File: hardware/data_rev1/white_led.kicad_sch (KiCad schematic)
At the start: 82 parts, among them U3 IS31FL3236A-TQ, U4 IS31FL3236A-TQ

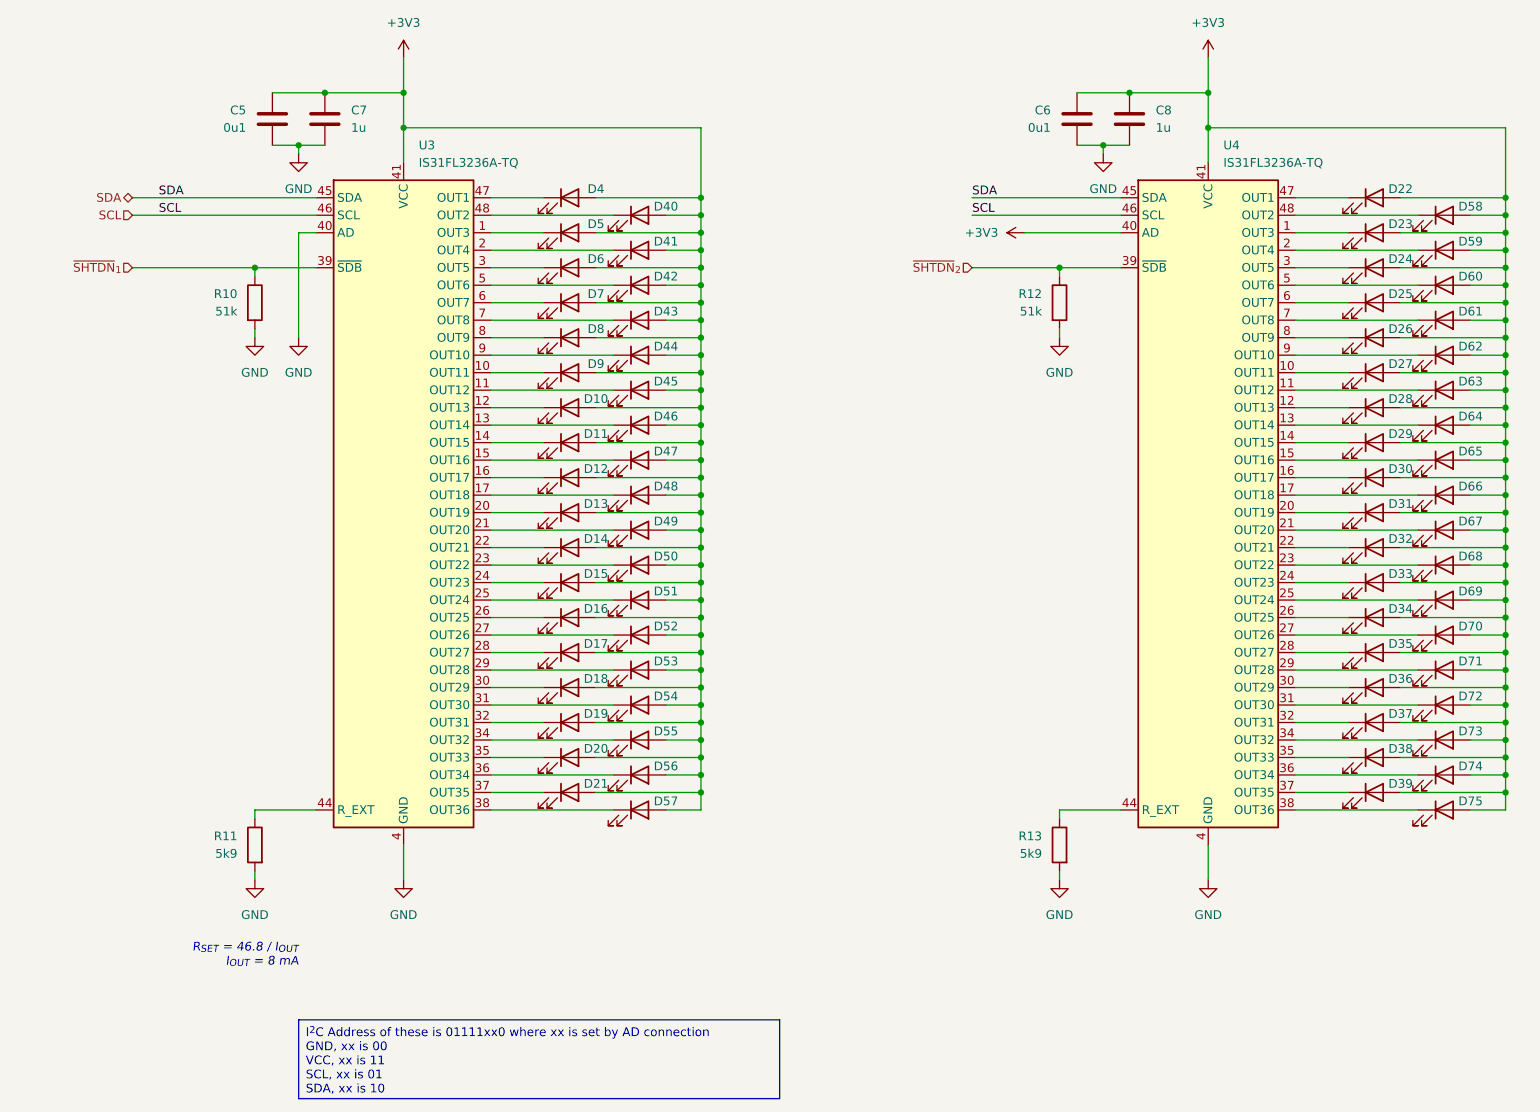
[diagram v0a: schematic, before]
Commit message: Added labels for LED lines
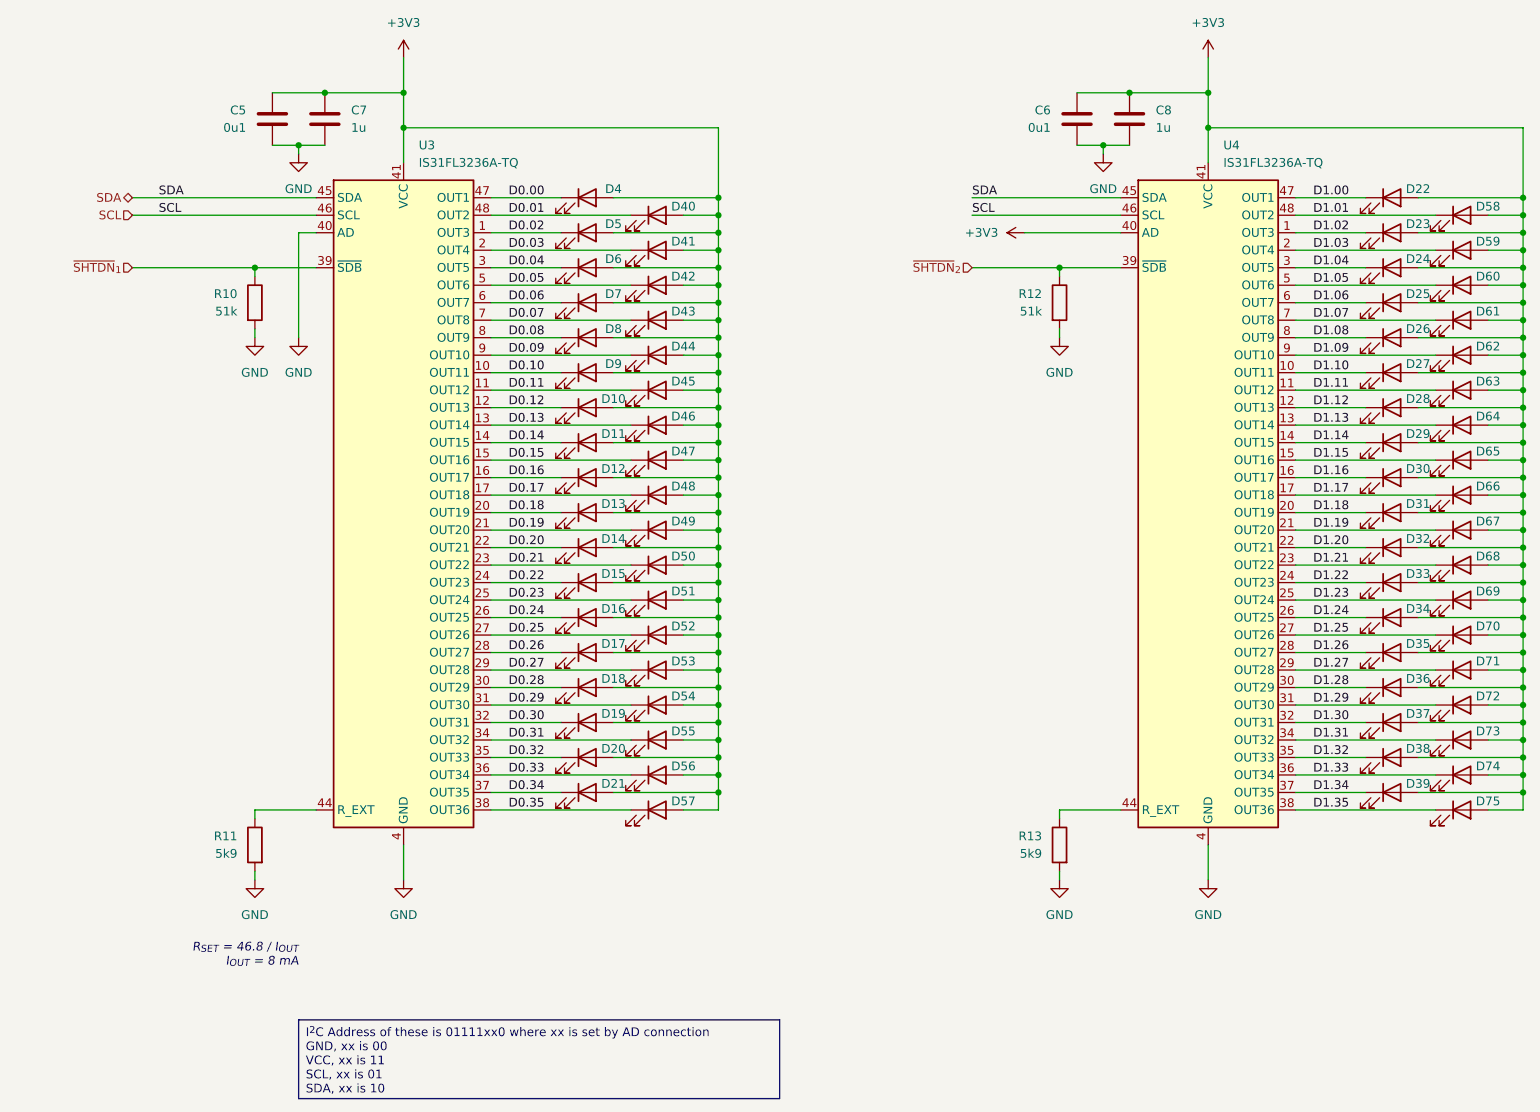
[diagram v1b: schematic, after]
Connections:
- net D0.19: now reaches D49.1 (K), U3.21 (OUT20)
- net D1.12: now reaches D28.1 (K), U4.12 (OUT13)
- net D0.20: now reaches D14.1 (K), U3.22 (OUT21)
- net D0.00: now reaches D4.1 (K), U3.47 (OUT1)
- net D0.11: now reaches D45.1 (K), U3.11 (OUT12)
- net D0.15: now reaches D47.1 (K), U3.15 (OUT16)
- net D1.09: now reaches D62.1 (K), U4.9 (OUT10)
- net D1.23: now reaches D69.1 (K), U4.25 (OUT24)
- net D1.25: now reaches D70.1 (K), U4.27 (OUT26)
- net D1.34: now reaches D39.1 (K), U4.37 (OUT35)
- net D1.00: now reaches D22.1 (K), U4.47 (OUT1)
- net D0.01: now reaches D40.1 (K), U3.48 (OUT2)
- net D1.03: now reaches D59.1 (K), U4.2 (OUT4)
- net D1.01: now reaches D58.1 (K), U4.48 (OUT2)
- net D0.31: now reaches D55.1 (K), U3.34 (OUT32)
- net D1.21: now reaches D68.1 (K), U4.23 (OUT22)
- net D1.13: now reaches D64.1 (K), U4.13 (OUT14)
- net D1.04: now reaches D24.1 (K), U4.3 (OUT5)
- net D0.12: now reaches D10.1 (K), U3.12 (OUT13)
- net D0.04: now reaches D6.1 (K), U3.3 (OUT5)
- net D0.30: now reaches D19.1 (K), U3.32 (OUT31)
- net D1.05: now reaches D60.1 (K), U4.5 (OUT6)
- net D1.22: now reaches D33.1 (K), U4.24 (OUT23)
- net D0.26: now reaches D17.1 (K), U3.28 (OUT27)
- net D0.03: now reaches D41.1 (K), U3.2 (OUT4)
- net D0.32: now reaches D20.1 (K), U3.35 (OUT33)
- net D1.24: now reaches D34.1 (K), U4.26 (OUT25)
- net D1.15: now reaches D65.1 (K), U4.15 (OUT16)
- net D0.17: now reaches D48.1 (K), U3.17 (OUT18)
- net D1.02: now reaches D23.1 (K), U4.1 (OUT3)
- net D0.28: now reaches D18.1 (K), U3.30 (OUT29)
- net D0.02: now reaches D5.1 (K), U3.1 (OUT3)
- net D0.10: now reaches D9.1 (K), U3.10 (OUT11)
- net D0.13: now reaches D46.1 (K), U3.13 (OUT14)
- net D0.14: now reaches D11.1 (K), U3.14 (OUT15)
- net D0.16: now reaches D12.1 (K), U3.16 (OUT17)
- net D0.18: now reaches D13.1 (K), U3.20 (OUT19)
- net D0.21: now reaches D50.1 (K), U3.23 (OUT22)
- net D0.22: now reaches D15.1 (K), U3.24 (OUT23)
- net D0.23: now reaches D51.1 (K), U3.25 (OUT24)
- net D0.24: now reaches D16.1 (K), U3.26 (OUT25)
- net D0.25: now reaches D52.1 (K), U3.27 (OUT26)
- net D0.27: now reaches D53.1 (K), U3.29 (OUT28)
- net D0.29: now reaches D54.1 (K), U3.31 (OUT30)
- net D0.33: now reaches D56.1 (K), U3.36 (OUT34)
- net D0.34: now reaches D21.1 (K), U3.37 (OUT35)
- net D0.35: now reaches D57.1 (K), U3.38 (OUT36)
- net D0.05: now reaches D42.1 (K), U3.5 (OUT6)
- net D0.06: now reaches D7.1 (K), U3.6 (OUT7)
- net D0.07: now reaches D43.1 (K), U3.7 (OUT8)
- net D0.08: now reaches D8.1 (K), U3.8 (OUT9)
- net D0.09: now reaches D44.1 (K), U3.9 (OUT10)
- net D1.30: now reaches D37.1 (K), U4.32 (OUT31)
- net D1.10: now reaches D27.1 (K), U4.10 (OUT11)
- net D1.08: now reaches D26.1 (K), U4.8 (OUT9)
- net D1.20: now reaches D32.1 (K), U4.22 (OUT21)
- net D1.29: now reaches D72.1 (K), U4.31 (OUT30)
- net D1.16: now reaches D30.1 (K), U4.16 (OUT17)
- net D1.31: now reaches D73.1 (K), U4.34 (OUT32)
- net D1.18: now reaches D31.1 (K), U4.20 (OUT19)
- net D1.32: now reaches D38.1 (K), U4.35 (OUT33)
- net D1.28: now reaches D36.1 (K), U4.30 (OUT29)
- net D1.06: now reaches D25.1 (K), U4.6 (OUT7)
- net D1.14: now reaches D29.1 (K), U4.14 (OUT15)
- net D1.27: now reaches D71.1 (K), U4.29 (OUT28)
- net D1.07: now reaches D61.1 (K), U4.7 (OUT8)
- net D1.33: now reaches D74.1 (K), U4.36 (OUT34)
- net D1.11: now reaches D63.1 (K), U4.11 (OUT12)
- net D1.17: now reaches D66.1 (K), U4.17 (OUT18)
- net D1.19: now reaches D67.1 (K), U4.21 (OUT20)
- net D1.26: now reaches D35.1 (K), U4.28 (OUT27)
- net D1.35: now reaches D75.1 (K), U4.38 (OUT36)
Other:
- moved on the sheet: D10, D11, D12, D13, D14, D15, D16, D17, D18, D19, D20, D21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
